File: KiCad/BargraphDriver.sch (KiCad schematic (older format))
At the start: 30 parts, among them Q1 Q_NPN_BEC, Q10 Q_NPN_BEC, Q2 Q_NPN_BEC, Q3 Q_NPN_BEC, Q4 Q_NPN_BEC, Q5 Q_NPN_BEC, Q6 Q_NPN_BEC, Q7 Q_NPN_BEC, Q8 Q_NPN_BEC, Q9 Q_NPN_BEC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

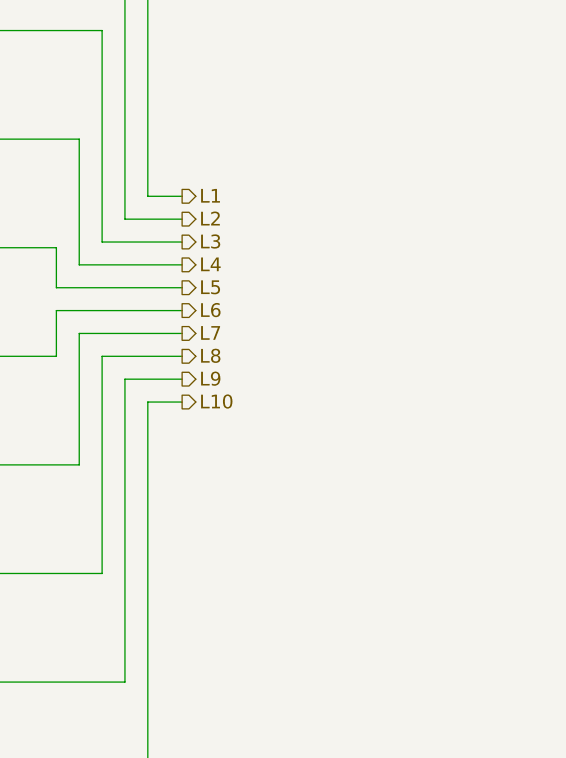
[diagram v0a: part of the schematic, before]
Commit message: New Mosfet designe Bargraph driver
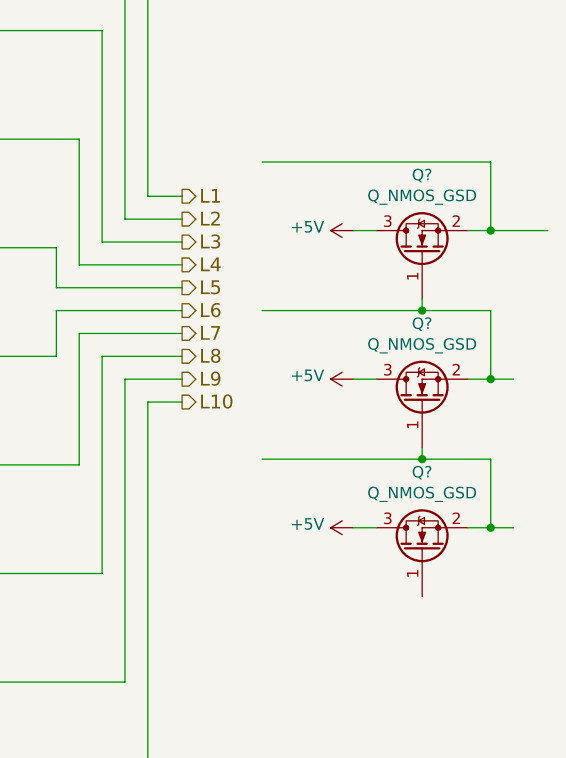
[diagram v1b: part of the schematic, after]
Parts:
- added Q? (x3): Q_NMOS_GSD, symbol Device:Q_NMOS_GSD
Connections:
- wire segments 112 -> 131
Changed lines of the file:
@@
 Wire Wire Line
 	5950 4950 6325 4950
+$Comp
+L Device:Q_NMOS_GSD Q?
+U 1 1 5B99FC59
+P 9950 3950
+F 0 "Q?" V 10293 3950 50  0000 C CNN
+F 1 "Q_NMOS_GSD" V 10202 3950 50  0000 C CNN
+F 2 "" H 10150 4050 50  0001 C CNN
+F 3 "~" H 9950 3950 50  0001 C CNN
+	1    9950 3950
+	0    -1   -1   0
+$EndComp
+$Comp
+L Device:Q_NMOS_GSD Q?
+U 1 1 5B99FE65
+P 9950 3300
+F 0 "Q?" V 10293 3300 50  0000 C CNN
+F 1 "Q_NMOS_GSD" V 10202 3300 50  0000 C CNN
+F 2 "" H 10150 3400 50  0001 C CNN
+F 3 "~" H 9950 3300 50  0001 C CNN
+	1    9950 3300
+	0    -1   -1   0
+$EndComp
+$Comp
+L power:+5V #PWR?
+U 1 1 5B99FF0A
+P 9650 3200
+F 0 "#PWR?" H 9650 3050 50  0001 C CNN
+F 1 "+5V" V 9665 3328 50  0000 L CNN
+F 2 "" H 9650 3200 50  0001 C CNN
+F 3 "" H 9650 3200 50  0001 C CNN
+	1    9650 3200
+	0    -1   -1   0
+$EndComp
+$Comp
+L power:+5V #PWR?
+U 1 1 5B99FFBC
+P 9650 3850
+F 0 "#PWR?" H 9650 3700 50  0001 C CNN
+F 1 "+5V" V 9665 3978 50  0000 L CNN
+F 2 "" H 9650 3850 50  0001 C CNN
+F 3 "" H 9650 3850 50  0001 C CNN
+	1    9650 3850
+	0    -1   -1   0
+$EndComp
+$Comp
+L power:+5V #PWR?
+U 1 1 5B9A0007
+P 9650 4500
+F 0 "#PWR?" H 9650 4350 50  0001 C CNN
+F 1 "+5V" V 9665 4628 50  0000 L CNN
+F 2 "" H 9650 4500 50  0001 C CNN
+F 3 "" H 9650 4500 50  0001 C CNN
+	1    9650 4500
+	0    -1   -1   0
+$EndComp
+$Comp
+L Device:Q_NMOS_GSD Q?
+U 1 1 5B9A0052
+P 9950 4600
+F 0 "Q?" V 10293 4600 50  0000 C CNN
+F 1 "Q_NMOS_GSD" V 10202 4600 50  0000 C CNN
+F 2 "" H 10150 4700 50  0001 C CNN
+F 3 "~" H 9950 4600 50  0001 C CNN
+	1    9950 4600
+	0    -1   -1   0
+$EndComp
+Wire Wire Line
+	9650 4500 9750 4500
+Wire Wire Line
+	9750 3850 9650 3850
+Wire Wire Line
+	9650 3200 9750 3200
+Wire Wire Line
+	9950 3500 9950 3550
+Wire Wire Line
+	9950 3550 10250 3550
+Wire Wire Line
+	10250 3550 10250 3850
+Wire Wire Line
+	10250 3850 10150 3850
+Wire Wire Line
+	10250 3850 10350 3850
+Connection ~ 10250 3850
+Wire Wire Line
+	10150 4500 10250 4500
+Wire Wire Line
+	10250 4500 10250 4200
+Wire Wire Line
+	10250 4200 9950 4200
+Wire Wire Line
+	9950 4200 9950 4150
+Wire Wire Line
+	10250 4500 10350 4500
+Connection ~ 10250 4500
+Wire Wire Line
+	10150 3200 10250 3200
+Wire Wire Line
+	10250 3200 10250 2900
+Connection ~ 10250 3200
+Wire Wire Line
+	10250 3200 10500 3200
+Wire Wire Line
+	9950 3550 9250 3550
+Connection ~ 9950 3550
+Wire Wire Line
+	9950 4200 9250 4200
+Connection ~ 9950 4200
+Wire Wire Line
+	9250 2900 10250 2900
 $EndSCHEMATC

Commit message: Bargraph driver - Mosfet
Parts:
- removed D10, D11, D12, D13, D5, D6, D7, D8, D9: D_Schottky, Diodes_SMD:SOD-123, symbol Device:D_Schottky
- removed Q1, Q10, Q2, Q3, Q4, Q5, Q6, Q7, Q8, Q9: Q_NPN_BEC, TO_SOT_Packages_SMD:SOT-23_Handsoldering, symbol Device:Q_NPN_BEC
- removed R28, R30, R35, R36, R37, R38, R39, R40, R41, R42: 125k, Resistors_SMD:R_0805_HandSoldering, symbol Device:R
- added D? (x9): D_Small, symbol Device:D_Small
- added Q? (x7): Q_NMOS_GSD, symbol Device:Q_NMOS_GSD
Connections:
- wire segments 131 -> 130
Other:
- moved on the sheet: Q?
